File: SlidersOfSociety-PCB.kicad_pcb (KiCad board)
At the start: 2 copper layers, 15 parts, among them J2 6P4C, J3 6P4C, J4 Conn_01x06_Pin, J5 Conn_01x08_Pin, SW1 219-4MST, SW2 limit switch, U1 PIC18F25K83-I/SO, U2 DRV8871DDA, U3 MCP2561-E-SN

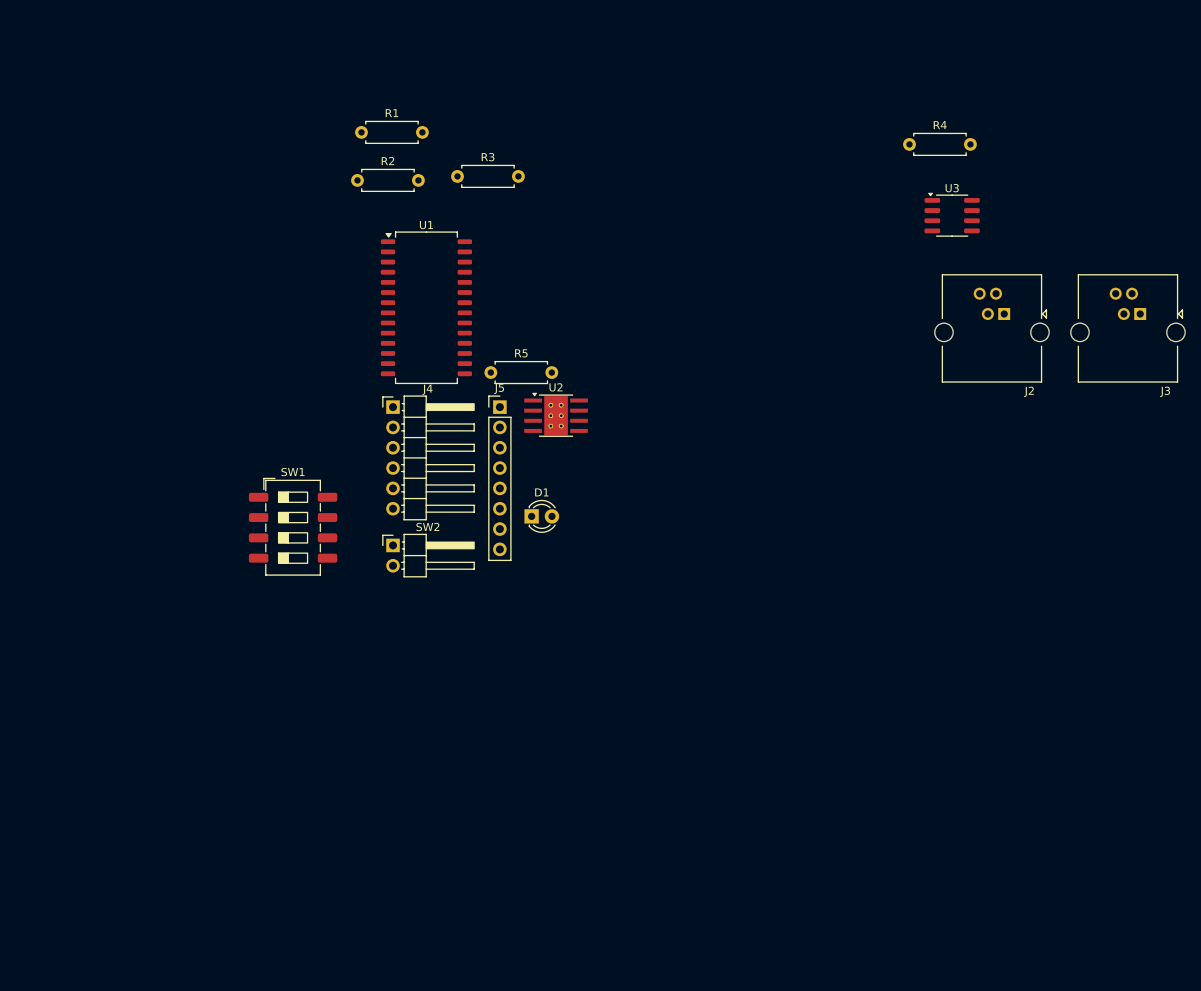
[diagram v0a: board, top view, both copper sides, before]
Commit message: add custom drc
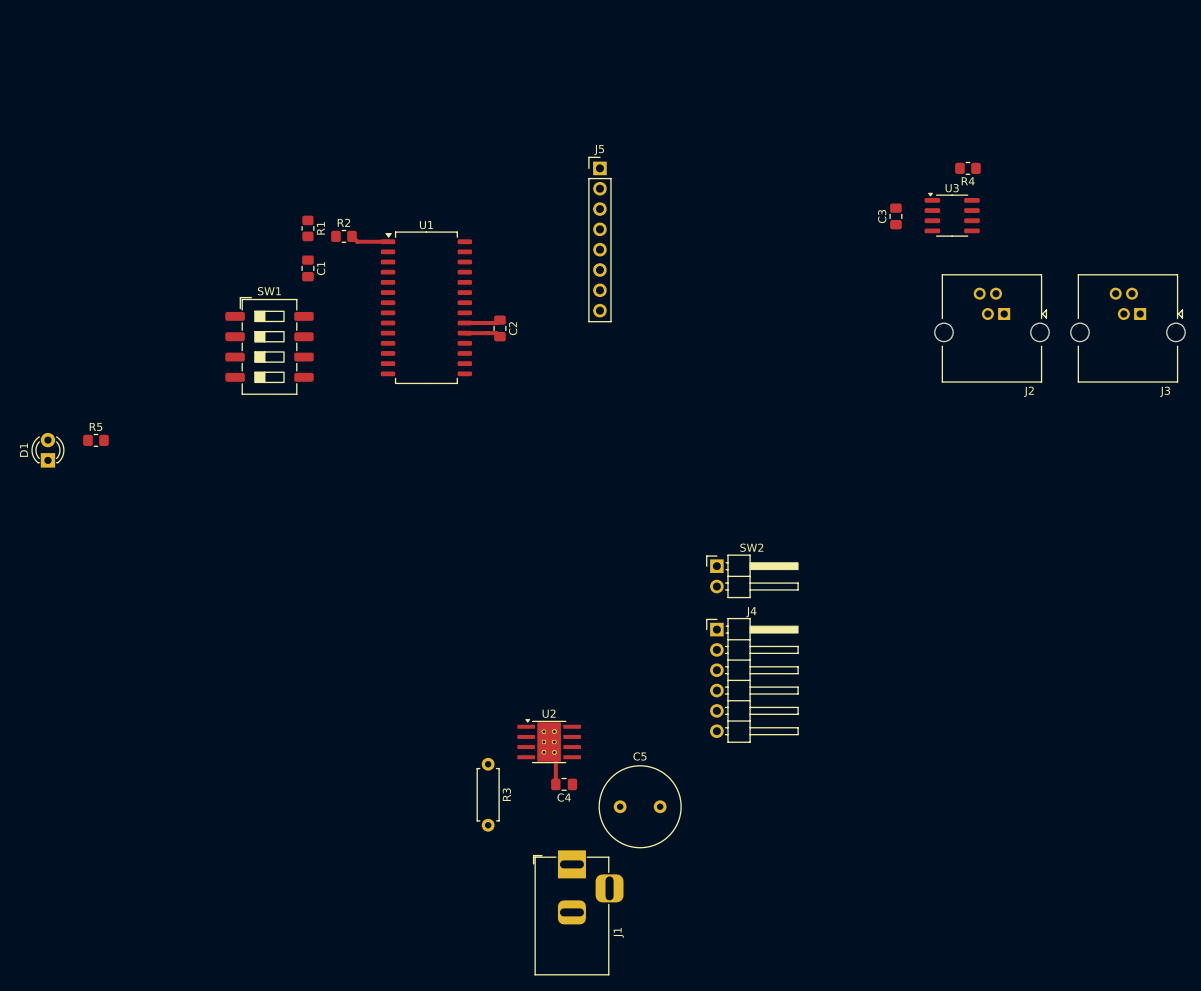
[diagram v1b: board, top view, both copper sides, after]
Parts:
- added C1: 1uF 20V, Capacitor_SMD:C_0805_2012Metric_Pad1.18x1.45mm_HandSolder, F.Cu at (123.0, 81.5)
- added C2: 1uF 20V, Capacitor_SMD:C_0805_2012Metric_Pad1.18x1.45mm_HandSolder, F.Cu at (147.0, 89.0)
- added C3: 0.1uF, Capacitor_SMD:C_0805_2012Metric_Pad1.18x1.45mm_HandSolder, F.Cu at (196.5, 75.0)
- added C4: 0.1uF, Capacitor_SMD:C_0805_2012Metric_Pad1.18x1.45mm_HandSolder, F.Cu at (155.0, 146.0)
- added C5: 47uF, Capacitor_THT:C_Radial_D10.0mm_H12.5mm_P5.00mm, F.Cu at (162.0, 148.8)
- added J1: Barrel_Jack_MountingPin, Connector_BarrelJack:BarrelJack_Horizontal, F.Cu at (156.0, 156.0)
- R1, R2, R4, R5: footprint Resistor_THT:R_Axial_DIN0207_L6.3mm_D2.5mm_P7.62mm_Horizontal -> Resistor_SMD:R_0805_2012Metric_Pad1.20x1.40mm_HandSolder
- moved R3 73.6 mm to (145.5, 143.5), turned to -90 degrees
- moved D1 60.9 mm to (90.5, 105.5), turned to 90 degrees
- moved R5 50.1 mm to (96.5, 103.0)
- moved J4 49.1 mm to (174.1, 126.7)
- moved U2 40.8 mm to (153.2, 140.7)
- moved SW2 40.6 mm to (174.1, 118.7)
- moved J5 32.4 mm to (159.5, 69.0)
- moved SW1 22.8 mm to (118.2, 91.3)
- moved R1 13.7 mm to (123.0, 76.5), turned to -90 degrees
- moved R4 7.90 mm to (205.5, 69.0), turned to 180 degrees
- moved R2 7.20 mm to (127.5, 77.5)
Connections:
- J4 pad 1: /QE1 -> QE1
- J4 pad 2: /QE2 -> QE2
- U1 pad 11: Net-(SW2-A) -> unconnected-(U1-RC0/SOSCO-Pad11)
- U1 pad 13: /QE1 -> unconnected-(U1-RC2-Pad13)
- U1 pad 14: /QE2 -> Net-(SW2-A)
- U1 pad 15: unconnected-(U1-RC4-Pad15) -> QE1
- U1 pad 16: unconnected-(U1-RC5-Pad16) -> QE2
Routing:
- net GND: track 0.00 -> 9.95 mm
- net Net-(U1-VPP/~{MCLR}/RE3): track 0.00 -> 4.79 mm
- net +5V: track 0.00 -> 4.54 mm

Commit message: finish pcb layout v0.2
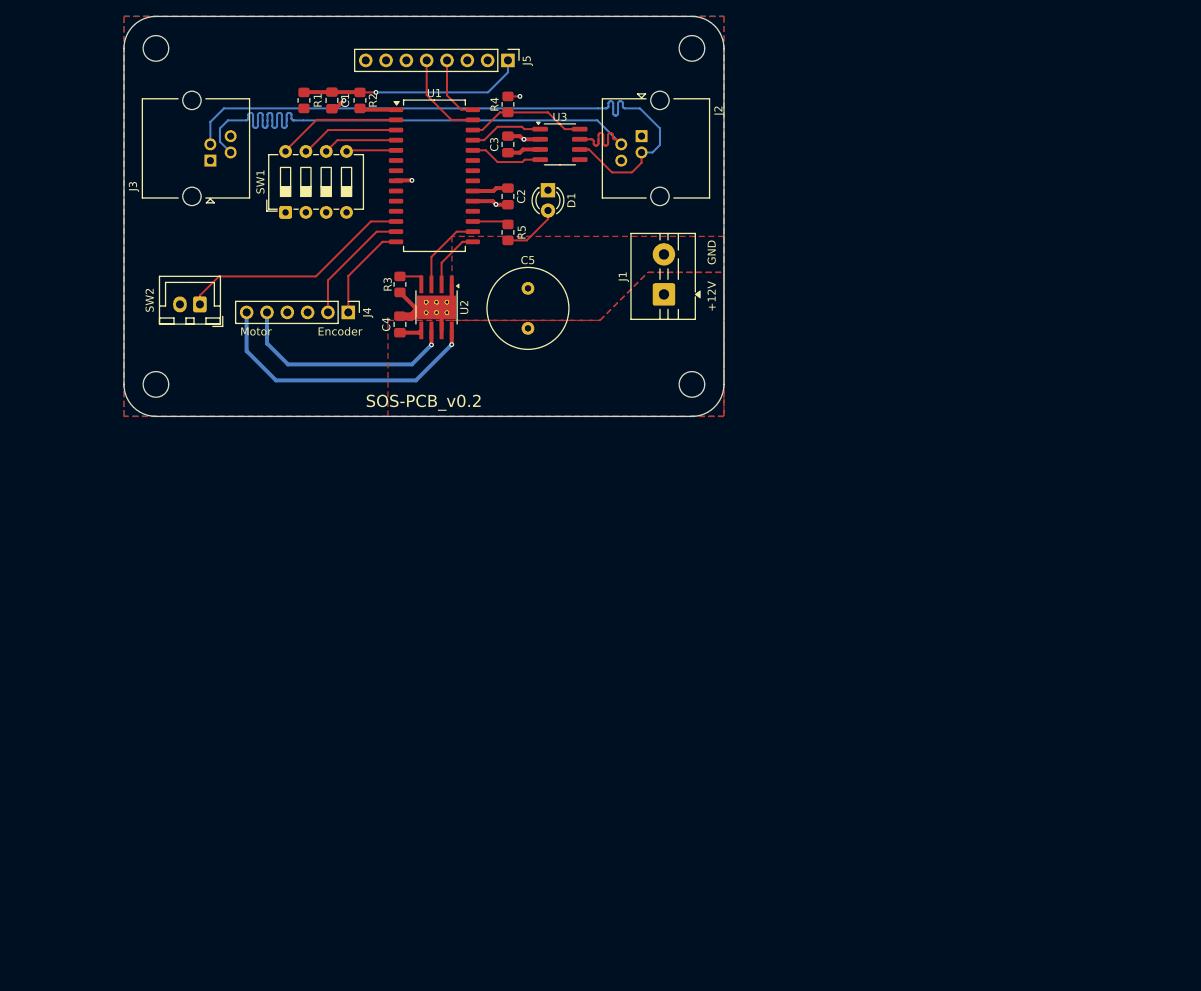
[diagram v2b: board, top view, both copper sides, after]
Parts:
- added REF**: MountingHole_3.2mm_M3_DIN965, MountingHole:MountingHole_3.2mm_M3_DIN965, F.Cu at (104.0, 54.0)
- added REF**: MountingHole_3.2mm_M3_DIN965, MountingHole:MountingHole_3.2mm_M3_DIN965, F.Cu at (171.0, 54.0)
- added REF**: MountingHole_3.2mm_M3_DIN965, MountingHole:MountingHole_3.2mm_M3_DIN965, F.Cu at (104.0, 96.0)
- added REF**: MountingHole_3.2mm_M3_DIN965, MountingHole:MountingHole_3.2mm_M3_DIN965, F.Cu at (171.0, 96.0)
- J1: value Barrel_Jack_MountingPin -> Screw_Terminal_01x02; footprint Connector_BarrelJack:BarrelJack_Horizontal -> TerminalBlock:TerminalBlock_MaiXu_MX126-5.0-02P_1x02_P5.00mm
- J4: footprint Connector_PinHeader_2.54mm:PinHeader_1x06_P2.54mm_Horizontal -> Connector_PinHeader_2.54mm:PinHeader_1x06_P2.54mm_Vertical
- R3: footprint Resistor_THT:R_Axial_DIN0207_L6.3mm_D2.5mm_P7.62mm_Horizontal -> Resistor_SMD:R_0805_2012Metric_Pad1.20x1.40mm_HandSolder
- SW1: value 219-4MST -> 210-4MS; footprint Button_Switch_SMD:SW_DIP_SPSTx04_Slide_6.7x11.72mm_W8.61mm_P2.54mm_LowProfile -> Button_Switch_THT:SW_DIP_SPSTx04_Slide_6.7x11.72mm_W7.62mm_P2.54mm_LowProfile
- SW2: footprint Connector_PinHeader_2.54mm:PinHeader_1x02_P2.54mm_Horizontal -> Connector_JST:JST_XH_B2B-XH-A_1x02_P2.50mm_Vertical
- moved J3 117.8 mm to (110.8, 68.0), turned to 90 degrees
- moved SW2 72.4 mm to (109.5, 86.0), turned to 180 degrees
- moved J1 72.2 mm to (167.5, 84.8)
- moved D1 71.0 mm to (153.0, 71.7), turned to -90 degrees
- moved C4 61.1 mm to (134.5, 88.5), turned to 90 degrees
- moved R3 61.0 mm to (134.5, 83.5)
- moved C5 60.9 mm to (150.5, 89.0), turned to 90 degrees
- moved J4 60.8 mm to (128.0, 87.0), turned to -90 degrees
- moved R4 58.1 mm to (148.0, 61.0), turned to 90 degrees
- moved R5 57.7 mm to (148.0, 77.0), turned to 90 degrees
- moved U2 56.1 mm to (139.1, 86.4), turned to -90 degrees
- moved J2 50.5 mm to (164.7, 65.0), turned to -90 degrees
- moved U3 49.8 mm to (154.5, 66.0)
- moved C3 49.3 mm to (148.0, 66.0)
- moved C1 21.2 mm to (126.0, 60.5)
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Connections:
- R5 pad 2: Net-(U1-RA4) -> Net-(U1-RC6)
- U1 pad 12: unconnected-(U1-RC1/SOSCI-Pad12) -> Net-(SW2-A)
- U1 pad 13: unconnected-(U1-RC2-Pad13) -> QE2
- U1 pad 14: Net-(SW2-A) -> QE1
- U1 pad 15: QE1 -> /MP2
- U1 pad 16: QE2 -> /MP1
- U1 pad 17: /MP1 -> Net-(U1-RC6)
- U1 pad 18: /MP2 -> unconnected-(U1-RC7-Pad18)
- U1 pad 23: /CANTX -> unconnected-(U1-RB2-Pad23)
- U1 pad 25: /CANSTBY -> /CANTX
- U1 pad 26: unconnected-(U1-RB5-Pad26) -> /CANSTBY
- U1 pad 6: Net-(U1-RA4) -> unconnected-(U1-RA4-Pad6)
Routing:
- net Net-(U3-CANL): track 0.00 -> 80.6 mm
- net Net-(U3-CANH): track 0.00 -> 80.4 mm
- net Net-(J4-Pin_6): track 0.00 -> 35.6 mm, vias 0 -> 1
- net Net-(SW2-A): track 0.00 -> 29.5 mm
- net Net-(J4-Pin_5): track 0.00 -> 28.3 mm, vias 0 -> 1
- net Net-(J5-Pin_1): track 0.00 -> 28.1 mm, vias 0 -> 1
- net GND: track 9.95 -> 29.1 mm, vias 0 -> 5
- net Net-(U1-RA0): track 0.00 -> 15.5 mm
- net /CANSTBY: track 0.00 -> 15.1 mm
- net QE2: track 0.00 -> 15.0 mm
- net Net-(U1-RA1): track 0.00 -> 12.4 mm
- net QE1: track 0.00 -> 12.3 mm
- net PGC: track 0.00 -> 11.4 mm
- net /MP1: track 0.00 -> 9.92 mm
- net Net-(U1-RA2): track 0.00 -> 9.37 mm
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- added copper zone on F.Cu, net +12V
- added copper zone on F.Cu, net +5V
- added copper zone on B.Cu, net GND
- added copper zone on F.Cu, net GND
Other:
- board outline added: 75 x 50 mm
- board text added: "+12V"
- board text added: "Encoder"
- board text added: "GND"
- board text added: "Motor"
- board text added: "SOS-PCB_v0.2"

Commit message: add branding
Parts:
- added G***: LOGO, LOGO, F.Cu at (159.0, 94.0)

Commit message: idk what changed here, been some time
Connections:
- U1 pad 10: unconnected-(U1-OSC2_CLKOUT/RA6-Pad10) -> Net-(SW2-A)
- U1 pad 12: Net-(SW2-A) -> unconnected-(U1-RC1/SOSCI-Pad12)
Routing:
- net Net-(SW2-A): track 29.5 -> 31.4 mm
